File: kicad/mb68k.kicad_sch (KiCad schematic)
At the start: 0 parts

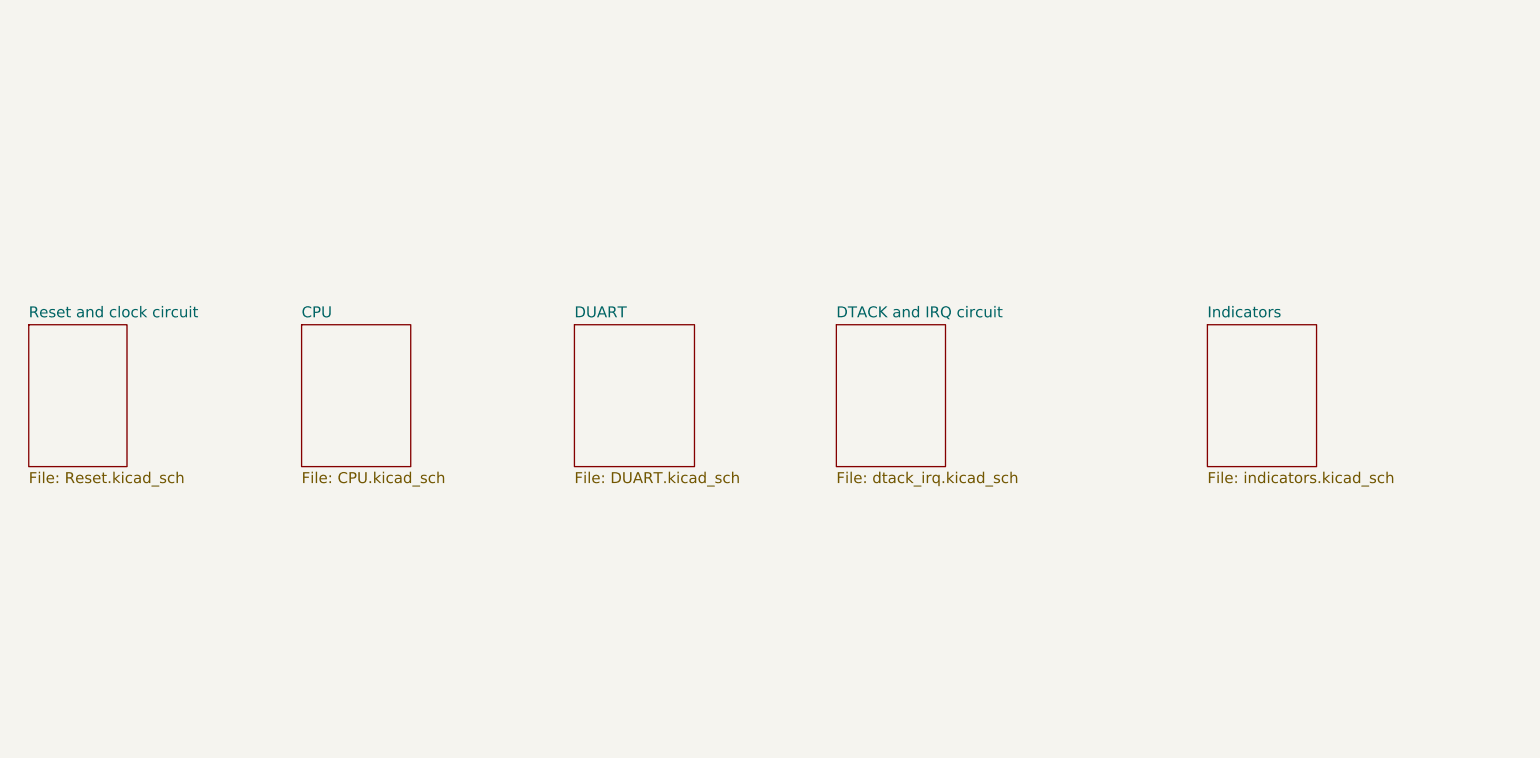
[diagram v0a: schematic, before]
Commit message: New decoding and GALs
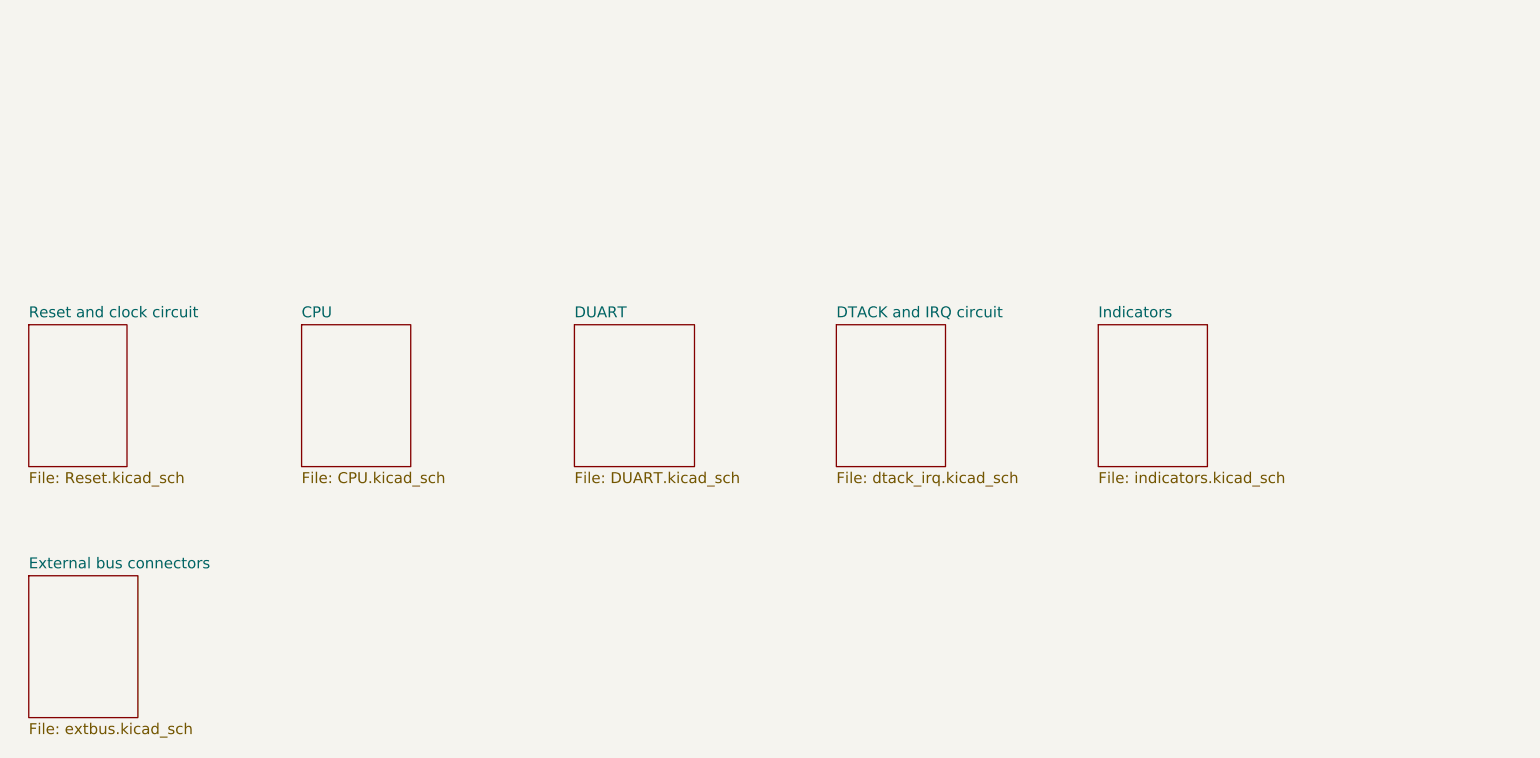
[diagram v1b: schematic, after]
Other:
- added sheet External bus connectors (extbus.kicad_sch)
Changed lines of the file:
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@@
     (rev "1.0-bboard")
   )
-  (sheet (at 195.58 64.77) (size 12.7 16.51) (fields_autoplaced)
+  (sheet (at 182.88 64.77) (size 12.7 16.51) (fields_autoplaced)
     (stroke (width 0.1524) (type solid))
     (fill (color 0 0 0 0.0000))
-    (property "Sheetname" "Indicators" (at 195.58 64.0584 0)
+    (property "Sheetname" "Indicators" (at 182.88 64.0584 0)
       (effects (font (size 1.27 1.27)) (justify left bottom))
     )
-    (property "Sheetfile" "indicators.kicad_sch" (at 195.58 81.8646 0)
+    (property "Sheetfile" "indicators.kicad_sch" (at 182.88 81.8646 0)
       (effects (font (size 1.27 1.27)) (justify left top))
     )
@@
       )
     )
+  )
+  (sheet (at 58.42 93.98) (size 12.7 16.51) (fields_autoplaced)
+    (stroke (width 0.1524) (type solid))
+    (fill (color 0 0 0 0.0000))
+    (property "Sheetname" "External bus connectors" (at 58.42 93.2684 0)
+      (effects (font (size 1.27 1.27)) (justify left bottom))
+    )
+    (property "Sheetfile" "extbus.kicad_sch" (at 58.42 111.0746 0)
+      (effects (font (size 1.27 1.27)) (justify left top))
+    )
+    (instances
+      (project "mb68k"
+        (path "/e63e39d7-6ac0-4ffd-8aa3-1841a4541b55" (page "7"))
+      )
+    )

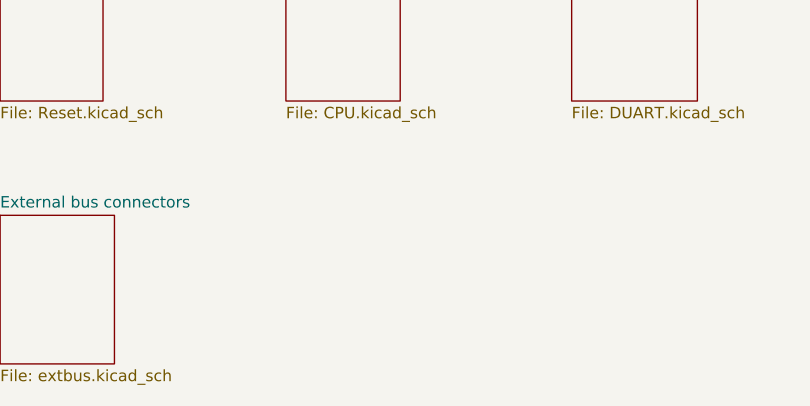
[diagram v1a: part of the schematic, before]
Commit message: Added Bus error handling
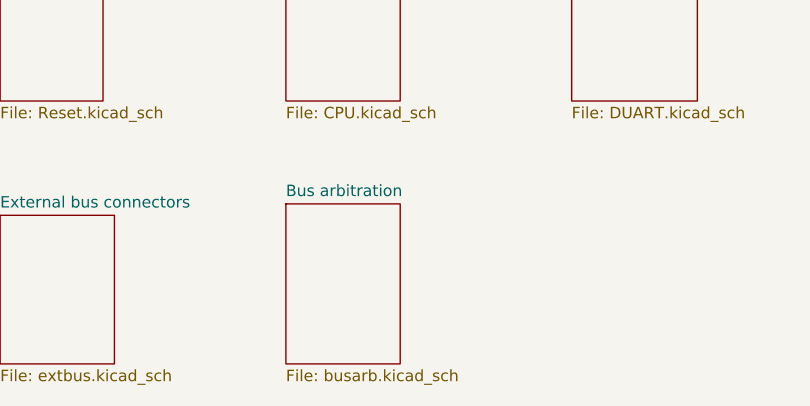
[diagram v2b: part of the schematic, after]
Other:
- added sheet Bus arbitration (busarb.kicad_sch)
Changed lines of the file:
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@@
+    )
+  )
+  (sheet (at 90.17 92.71) (size 12.7 17.78) (fields_autoplaced)
+    (stroke (width 0.1524) (type solid))
+    (fill (color 0 0 0 0.0000))
+    (property "Sheetname" "Bus arbitration" (at 90.17 91.9984 0)
+      (effects (font (size 1.27 1.27)) (justify left bottom))
+    )
+    (property "Sheetfile" "busarb.kicad_sch" (at 90.17 111.0746 0)
+      (effects (font (size 1.27 1.27)) (justify left top))
+    )
+    (instances
+      (project "mb68k"
+        (path "/e63e39d7-6ac0-4ffd-8aa3-1841a4541b55" (page "8"))
+      )
     )
   )

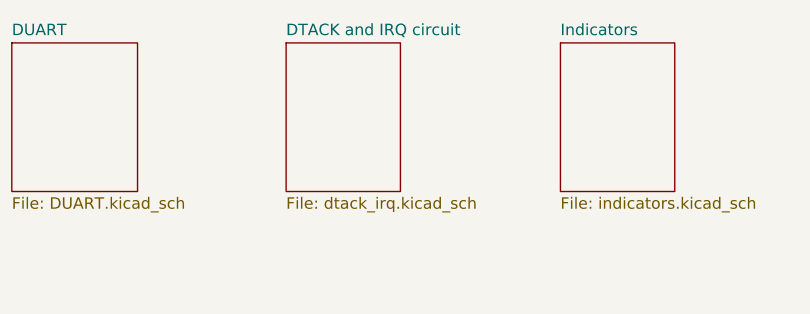
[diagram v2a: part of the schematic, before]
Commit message: finalized signaling PLD
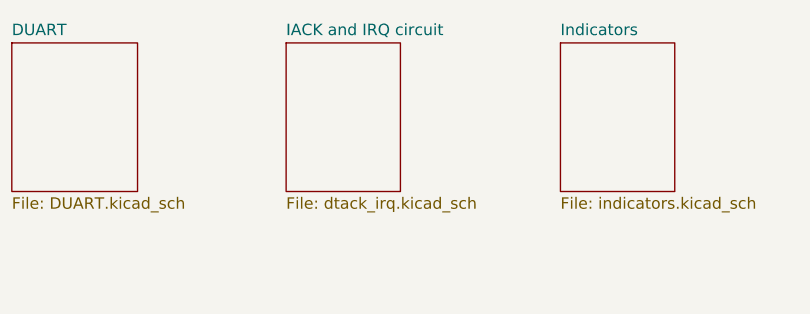
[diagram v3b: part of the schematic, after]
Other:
- sheet DTACK and IRQ circuit renamed IACK and IRQ circuit
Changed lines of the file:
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@@
     (stroke (width 0.1524) (type solid))
     (fill (color 0 0 0 0.0000))
-    (property "Sheetname" "DTACK and IRQ circuit" (at 152.4 64.0584 0)
+    (property "Sheetname" "IACK and IRQ circuit" (at 152.4 64.0584 0)
       (effects (font (size 1.27 1.27)) (justify left bottom))
     )

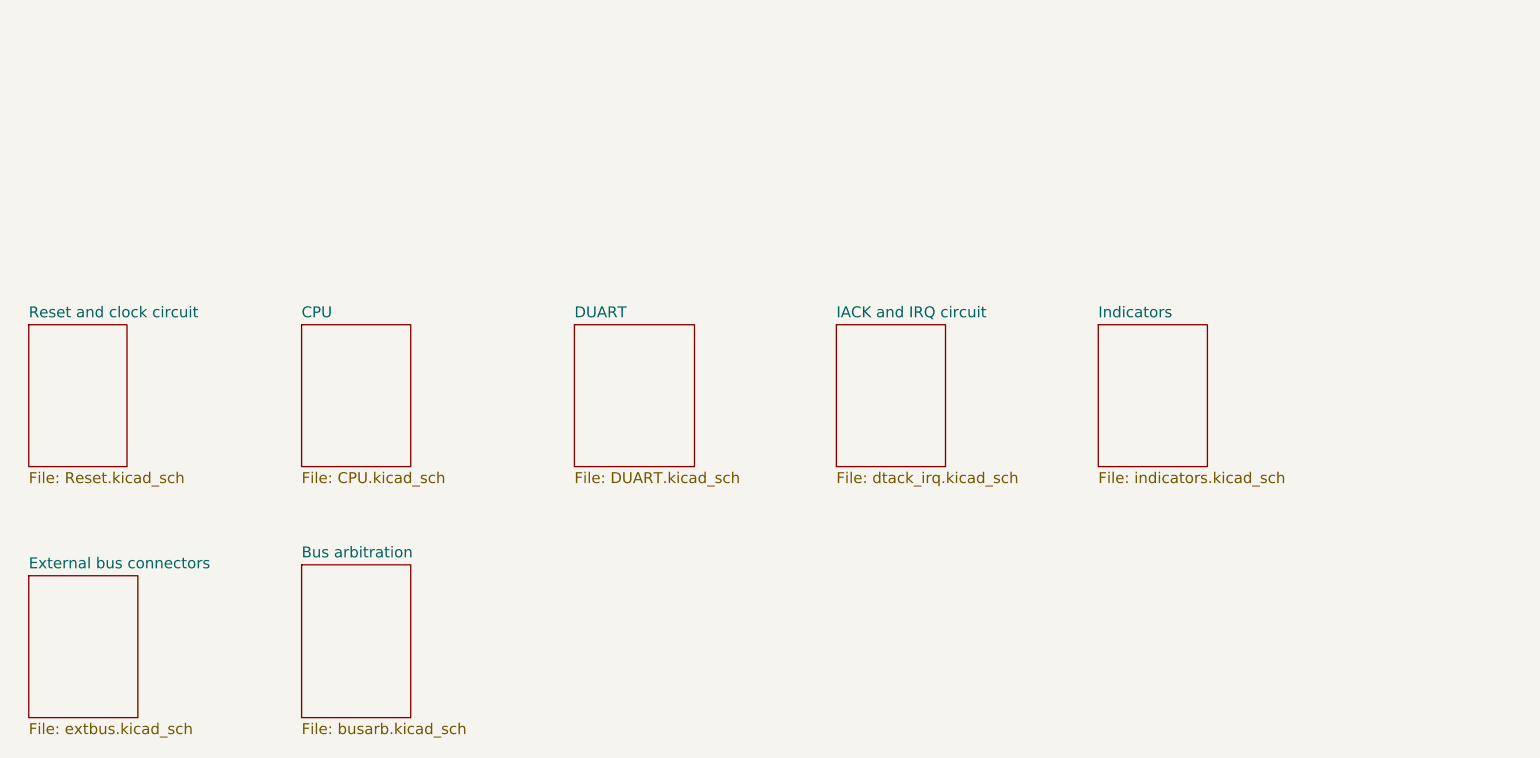
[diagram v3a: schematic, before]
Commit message: PCB to ATX size
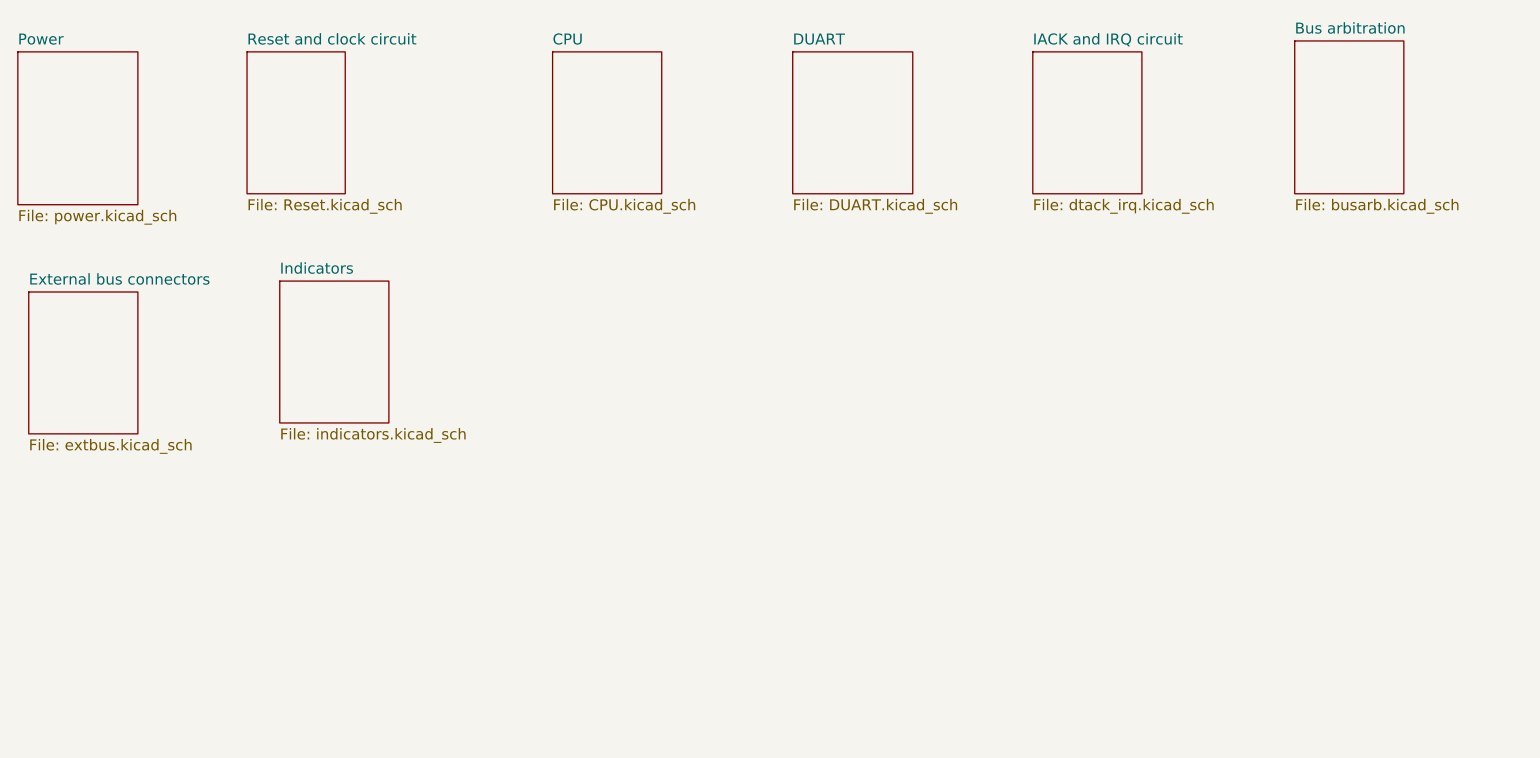
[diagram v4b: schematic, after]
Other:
- added sheet Power (power.kicad_sch)
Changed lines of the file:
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@@
     (rev "1.0-bboard")
   )
-  (sheet (at 182.88 64.77) (size 12.7 16.51) (fields_autoplaced)
+  (sheet (at 87.63 59.69) (size 12.7 16.51) (fields_autoplaced)
     (stroke (width 0.1524) (type solid))
     (fill (color 0 0 0 0.0000))
-    (property "Sheetname" "Indicators" (at 182.88 64.0584 0)
+    (property "Sheetname" "Indicators" (at 87.63 58.9784 0)
       (effects (font (size 1.27 1.27)) (justify left bottom))
     )
-    (property "Sheetfile" "indicators.kicad_sch" (at 182.88 81.8646 0)
+    (property "Sheetfile" "indicators.kicad_sch" (at 87.63 76.7846 0)
       (effects (font (size 1.27 1.27)) (justify left top))
     )
@@
     )
   )
-  (sheet (at 58.42 64.77) (size 11.43 16.51) (fields_autoplaced)
+  (sheet (at 83.82 33.02) (size 11.43 16.51) (fields_autoplaced)
     (stroke (width 0.1524) (type solid))
     (fill (color 0 0 0 0.0000))
-    (property "Sheetname" "Reset and clock circuit" (at 58.42 64.0584 0)
+    (property "Sheetname" "Reset and clock circuit" (at 83.82 32.3084 0)
       (effects (font (size 1.27 1.27)) (justify left bottom))
     )
-    (property "Sheetfile" "Reset.kicad_sch" (at 58.42 81.8646 0)
+    (property "Sheetfile" "Reset.kicad_sch" (at 83.82 50.1146 0)
       (effects (font (size 1.27 1.27)) (justify left top))
     )
@@
     )
   )
-  (sheet (at 58.42 93.98) (size 12.7 16.51) (fields_autoplaced)
+  (sheet (at 58.42 60.96) (size 12.7 16.51) (fields_autoplaced)
     (stroke (width 0.1524) (type solid))
     (fill (color 0 0 0 0.0000))
-    (property "Sheetname" "External bus connectors" (at 58.42 93.2684 0)
+    (property "Sheetname" "External bus connectors" (at 58.42 60.2484 0)
       (effects (font (size 1.27 1.27)) (justify left bottom))
     )
-    (property "Sheetfile" "extbus.kicad_sch" (at 58.42 111.0746 0)
+    (property "Sheetfile" "extbus.kicad_sch" (at 58.42 78.0546 0)
       (effects (font (size 1.27 1.27)) (justify left top))
     )
@@
     )
   )
-  (sheet (at 90.17 92.71) (size 12.7 17.78) (fields_autoplaced)
+  (sheet (at 57.15 33.02) (size 13.97 17.78) (fields_autoplaced)
     (stroke (width 0.1524) (type solid))
     (fill (color 0 0 0 0.0000))
-    (property "Sheetname" "Bus arbitration" (at 90.17 91.9984 0)
+    (property "Sheetname" "Power" (at 57.15 32.3084 0)
       (effects (font (size 1.27 1.27)) (justify left bottom))
     )
-    (property "Sheetfile" "busarb.kicad_sch" (at 90.17 111.0746 0)
+    (property "Sheetfile" "power.kicad_sch" (at 57.15 51.3846 0)
       (effects (font (size 1.27 1.27)) (justify left top))
     )
     (instances
       (project "mb68k"
-        (path "/e63e39d7-6ac0-4ffd-8aa3-1841a4541b55" (page "8"))
+        (path "/e63e39d7-6ac0-4ffd-8aa3-1841a4541b55" (page "1"))
       )
     )
   )
-  (sheet (at 90.17 64.77) (size 12.7 16.51) (fields_autoplaced)
+  (sheet (at 205.74 31.75) (size 12.7 17.78) (fields_autoplaced)
     (stroke (width 0.1524) (type solid))
     (fill (color 0 0 0 0.0000))
-    (property "Sheetname" "CPU" (at 90.17 64.0584 0)
+    (property "Sheetname" "Bus arbitration" (at 205.74 31.0384 0)
       (effects (font (size 1.27 1.27)) (justify left bottom))
     )
-    (property "Sheetfile" "CPU.kicad_sch" (at 90.17 81.8646 0)
+    (property "Sheetfile" "busarb.kicad_sch" (at 205.74 50.1146 0)
+      (effects (font (size 1.27 1.27)) (justify left top))
+    )
+    (instances
+      (project "mb68k"
+        (path "/e63e39d7-6ac0-4ffd-8aa3-1841a4541b55" (page "6"))
+      )
+    )
+  )
+  (sheet (at 119.38 33.02) (size 12.7 16.51) (fields_autoplaced)
+    (stroke (width 0.1524) (type solid))
+    (fill (color 0 0 0 0.0000))
+    (property "Sheetname" "CPU" (at 119.38 32.3084 0)
+      (effects (font (size 1.27 1.27)) (justify left bottom))
+    )
+    (property "Sheetfile" "CPU.kicad_sch" (at 119.38 50.1146 0)
       (effects (font (size 1.27 1.27)) (justify left top))
     )
@@
     )
   )
-  (sheet (at 121.92 64.77) (size 13.97 16.51) (fields_autoplaced)
+  (sheet (at 147.32 33.02) (size 13.97 16.51) (fields_autoplaced)
     (stroke (width 0.1524) (type solid))
     (fill (color 0 0 0 0.0000))
-    (property "Sheetname" "DUART" (at 121.92 64.0584 0)
+    (property "Sheetname" "DUART" (at 147.32 32.3084 0)
       (effects (font (size 1.27 1.27)) (justify left bottom))
     )
-    (property "Sheetfile" "DUART.kicad_sch" (at 121.92 81.8646 0)
+    (property "Sheetfile" "DUART.kicad_sch" (at 147.32 50.1146 0)
       (effects (font (size 1.27 1.27)) (justify left top))
     )
@@
     )
   )
-  (sheet (at 152.4 64.77) (size 12.7 16.51) (fields_autoplaced)
+  (sheet (at 175.26 33.02) (size 12.7 16.51) (fields_autoplaced)
     (stroke (width 0.1524) (type solid))
     (fill (color 0 0 0 0.0000))
-    (property "Sheetname" "IACK and IRQ circuit" (at 152.4 64.0584 0)
+    (property "Sheetname" "IACK and IRQ circuit" (at 175.26 32.3084 0)
       (effects (font (size 1.27 1.27)) (justify left bottom))
     )
-    (property "Sheetfile" "dtack_irq.kicad_sch" (at 152.4 81.8646 0)
+    (property "Sheetfile" "dtack_irq.kicad_sch" (at 175.26 50.1146 0)
       (effects (font (size 1.27 1.27)) (justify left top))
     )

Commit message: got irq to work
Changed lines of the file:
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@@
     (rev "1.0-bboard")
   )
-  (sheet (at 87.63 59.69) (size 12.7 16.51) (fields_autoplaced)
+  (sheet (at 87.63 60.96) (size 12.7 16.51) (fields_autoplaced)
     (stroke (width 0.1524) (type solid))
     (fill (color 0 0 0 0.0000))
-    (property "Sheetname" "Indicators" (at 87.63 58.9784 0)
+    (property "Sheetname" "Indicators" (at 87.63 60.2484 0)
       (effects (font (size 1.27 1.27)) (justify left bottom))
     )
-    (property "Sheetfile" "indicators.kicad_sch" (at 87.63 76.7846 0)
+    (property "Sheetfile" "indicators.kicad_sch" (at 87.63 78.0546 0)
       (effects (font (size 1.27 1.27)) (justify left top))
     )
